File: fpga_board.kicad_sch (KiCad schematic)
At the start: 180 parts, among them Q1 2N7002PW, Q2 2N7002PW, Q3 2N7002PW, Q4 2N7002PW, Q5 2N7002PW, Q6 2N7002PW, SW1 1TS028A-1300-0600-CT, U1 LFE5U-45F-7BG256I, U10 TLV62569DRL, U2 CYUSB3014-BZXC, U3 TLV62569DRL, U5 K4B4G1646E-BCMA, U6 K4B4G1646E-BCMA, U7 TLV62569DRL, U8 TLV62569DRL, U9 TLV62569DRL, X1 XO32, Y1 Crystal_GND24

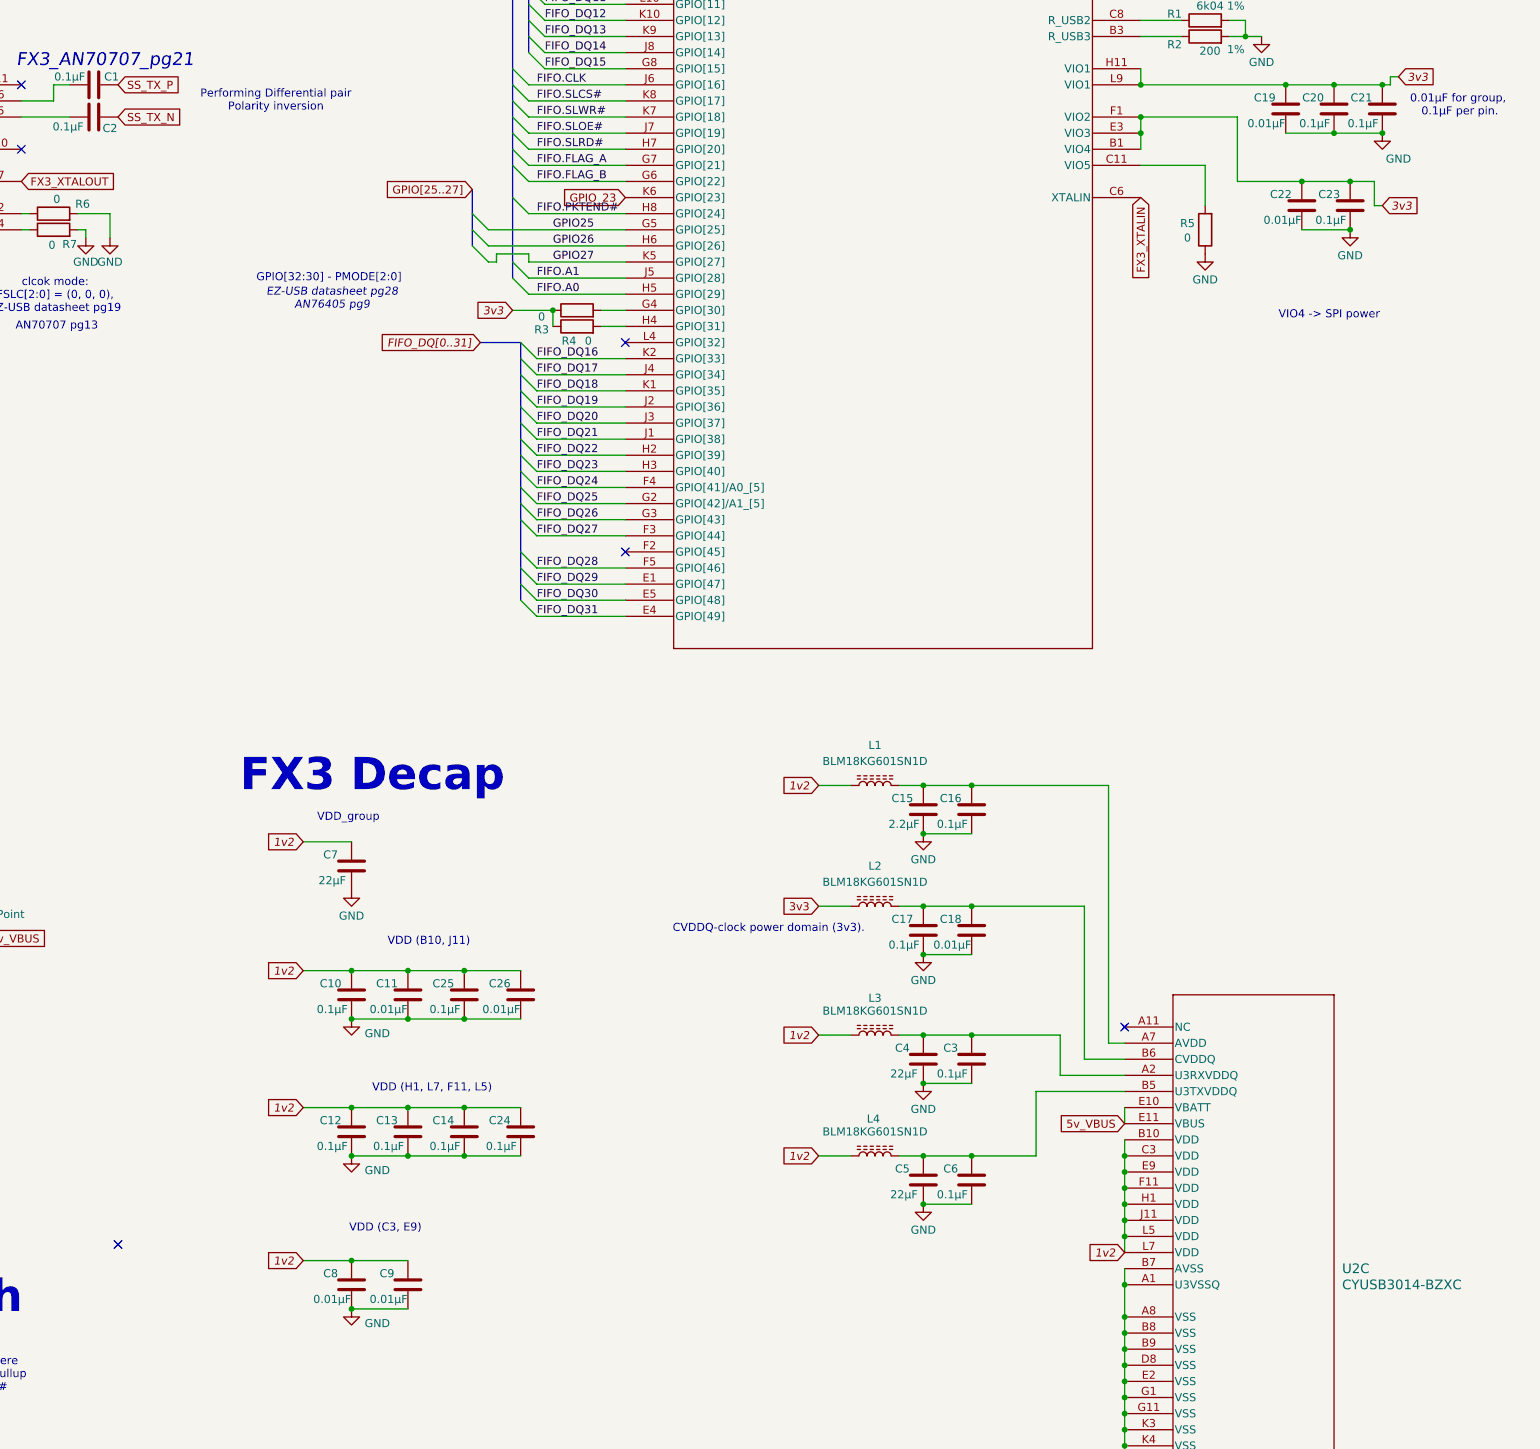
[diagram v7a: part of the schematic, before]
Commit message: added FX3 decaps (no power yet).
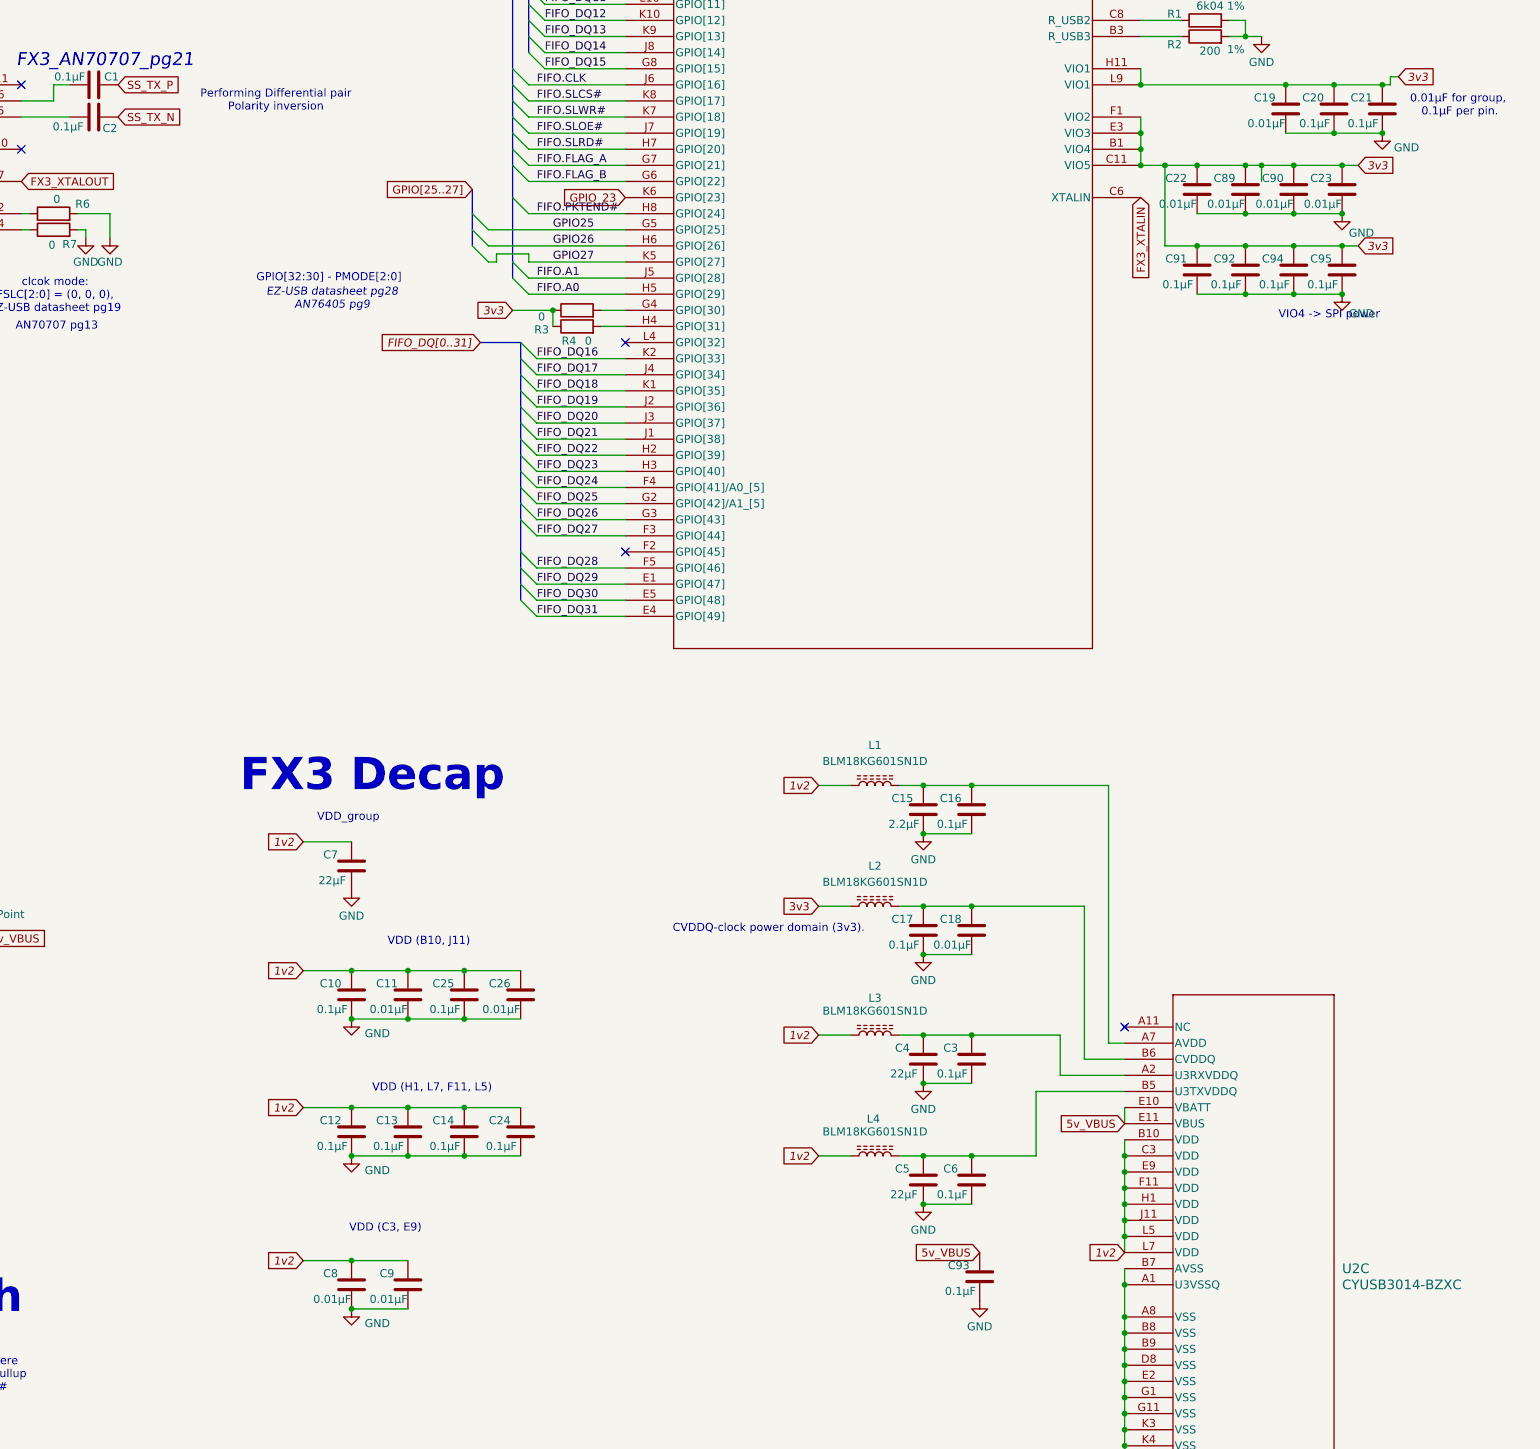
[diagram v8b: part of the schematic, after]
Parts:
- removed R5: 0, Resistor_SMD:R_0402_1005Metric, symbol Device:R
- added C89, C90: 0.01µF, Capacitor_SMD:C_0402_1005Metric, symbol Device:C
- added C91, C92, C93, C94, C95: 0.1µF, Capacitor_SMD:C_0402_1005Metric, symbol Device:C
- C23: value 0.1µF -> 0.01µF
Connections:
- net 3v3: now also U2.C11 (VIO5), C89.2, C90.2, C91.2, C92.2, C94.2, C95.2
- net 5v_VBUS: now also C93.2
- net GND: now also C89.1, C90.1, C91.1, C92.1, C93.1, C94.1, C95.1
- no-connect marks 74 -> 73
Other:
- moved on the sheet: C22
